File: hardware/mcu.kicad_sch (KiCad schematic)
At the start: 27 parts, among them IC1 R7FA4M1AB3CFM#AA0

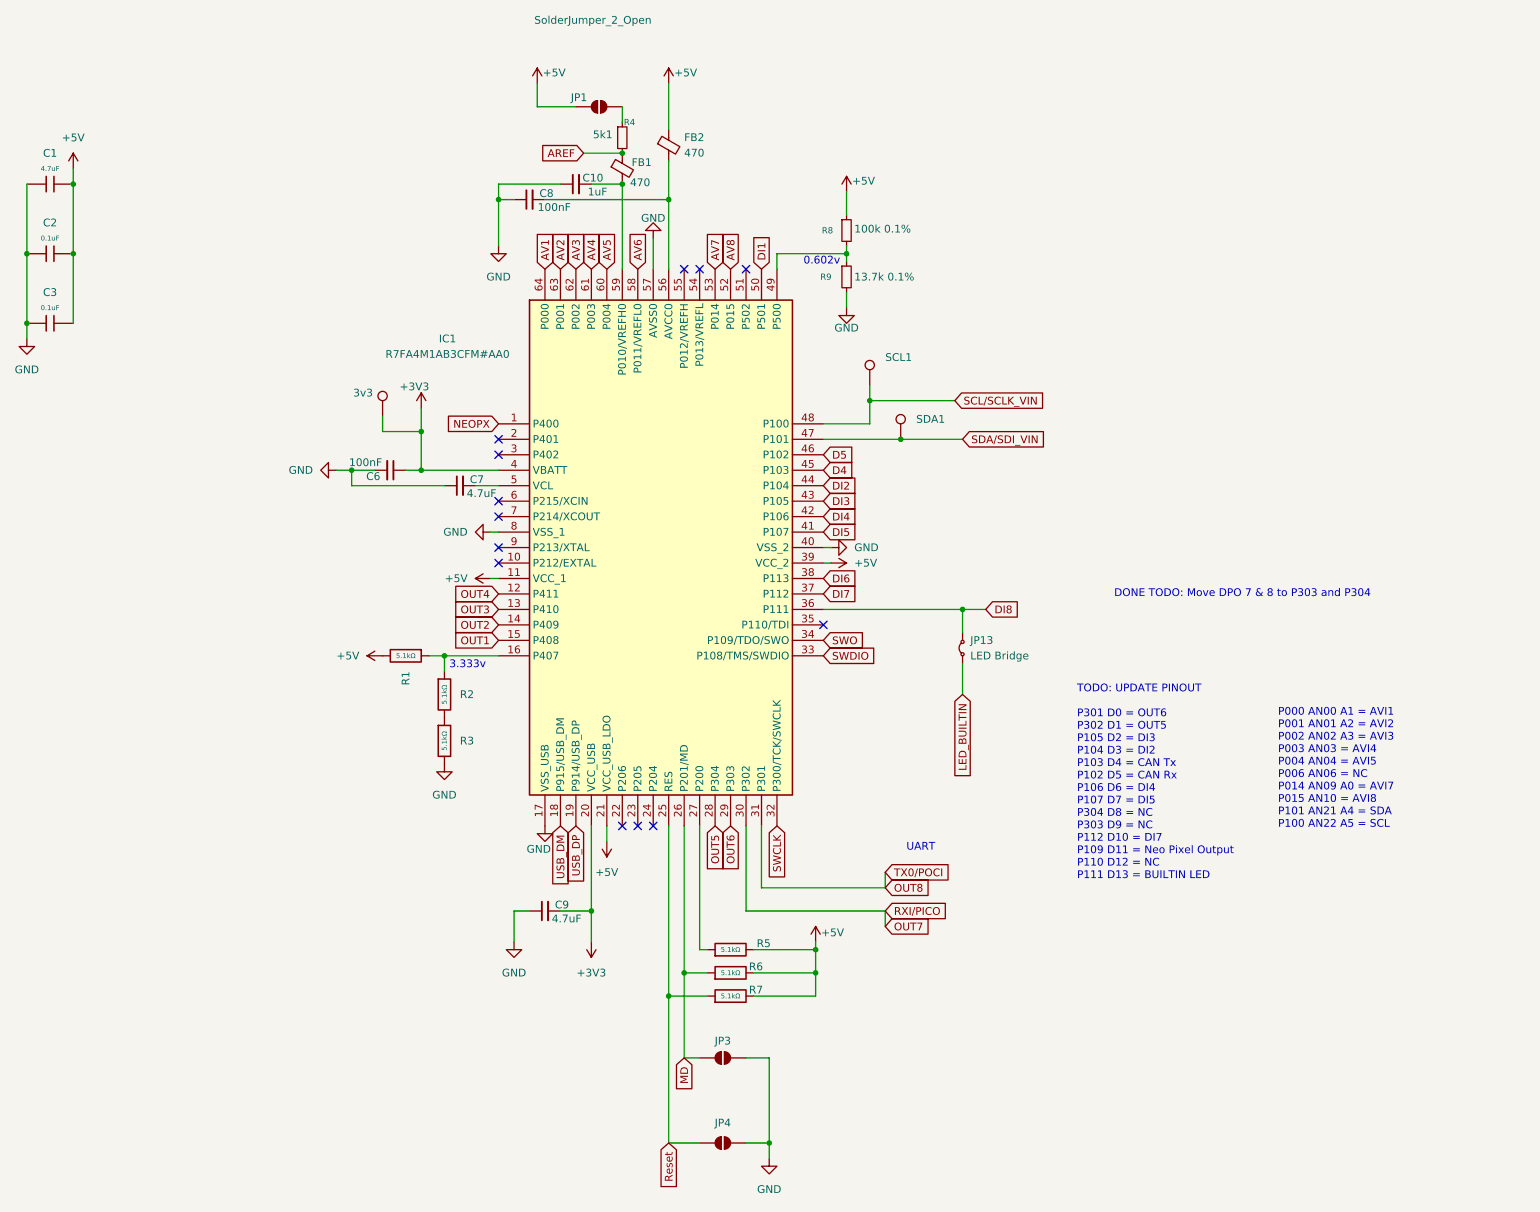
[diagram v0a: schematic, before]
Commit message: wire up altimeter, temp, barometer, imu, gps to MCU
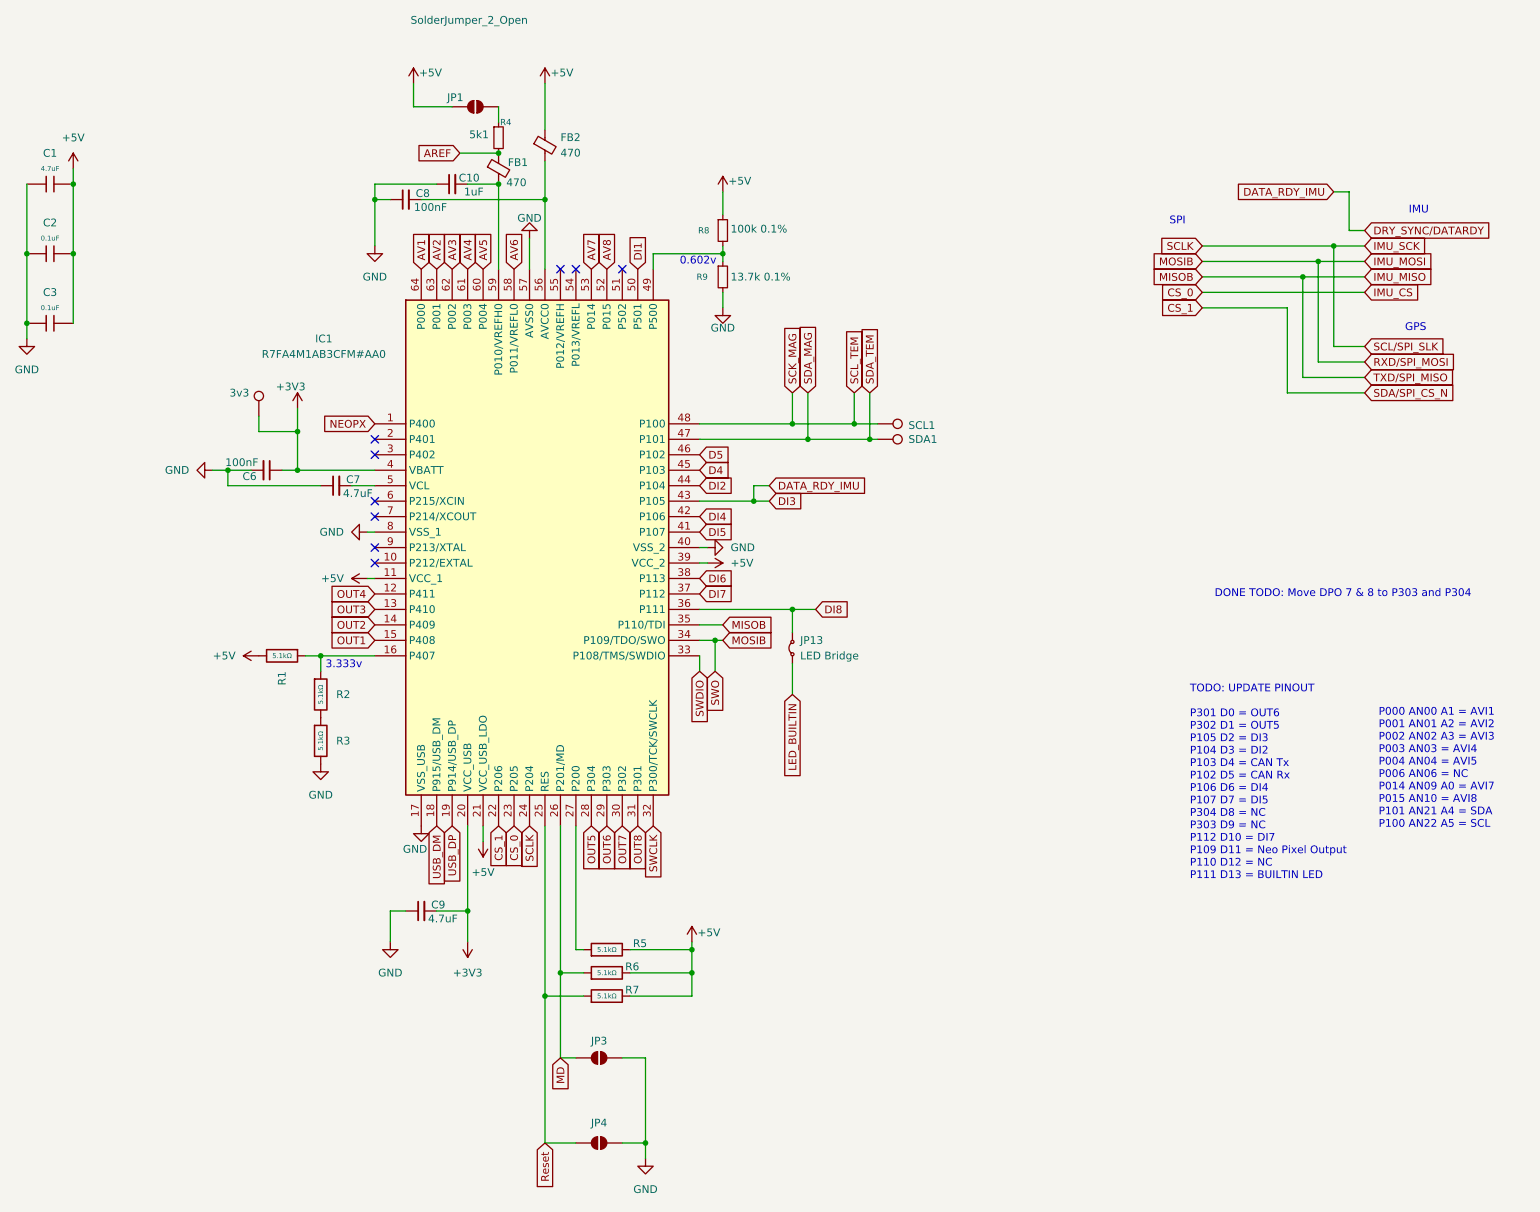
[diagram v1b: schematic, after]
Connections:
- net CS_1: now reaches IC1.22 (P206)
- net CS_0: now reaches IC1.23 (P205)
- net IMU_SCK: now reaches IC1.24 (P204)
- net IMU_MISO: now reaches IC1.35 (P110/TDI)
- net DI3 renamed DATA_RDY_IMU
- net SCL/SCLK_VIN renamed SCK_MAG
- net SDA/SDI_VIN renamed SDA_MAG
- net SWO renamed IMU_MOSI
- no-connect marks 13 -> 9
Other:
- note added: "GPS"
- note added: "IMU"
- note added: "SPI"
- note removed: "UART"
- moved on the sheet: 3v3, C10, C6, C7, C8, C9, FB1, FB2, IC1, JP1, JP13, JP3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
